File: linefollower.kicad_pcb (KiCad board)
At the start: 2 copper layers, 0 parts

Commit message: Minor schematic fixes - now RC; Basic PCB
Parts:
- added C1: 10uF, Capacitor_SMD:CP_Elec_5x5.3, F.Cu at (53.3, 119.5)
- added C10: 100uF, Capacitor_SMD:CP_Elec_6.3x5.4, F.Cu at (375.3, 51.8)
- added C11: 10uF, Capacitor_SMD:CP_Elec_5x5.3, F.Cu at (135.9, 125.1)
- added C12: 22pF, Capacitor_SMD:C_0805_2012Metric, F.Cu at (401.0, 43.1)
- added C13: 22pF, Capacitor_SMD:C_0805_2012Metric, F.Cu at (401.3, 34.8)
- added C14: 2.2uF, Capacitor_SMD:C_0805_2012Metric, F.Cu at (378.8, 65.0)
- added C15: 2.2uF, Capacitor_SMD:C_0805_2012Metric, F.Cu at (385.5, 58.9)
- added C16: 100nF, Capacitor_SMD:C_0805_2012Metric, F.Cu at (380.2, 61.1)
- added C17: 100nF, Capacitor_SMD:C_0805_2012Metric, F.Cu at (356.3, 78.1)
- added C18: 100nF, Capacitor_SMD:C_0805_2012Metric, F.Cu at (402.7, 32.8)
- added C19: 100nF, Capacitor_SMD:C_0805_2012Metric, F.Cu at (371.2, 68.0)
- added C2: 10uF, Capacitor_SMD:CP_Elec_5x5.3, F.Cu at (384.1, 51.1)
- added C20: 100nF, Capacitor_SMD:C_0805_2012Metric, F.Cu at (363.1, 78.4)
- added C21: 100nF, Capacitor_SMD:C_0805_2012Metric, F.Cu at (389.8, 48.9)
- added C22: 100nF, Capacitor_SMD:C_0805_2012Metric, F.Cu at (401.3, 38.7)
- added C23: 100nF, Capacitor_SMD:C_0805_2012Metric, F.Cu at (401.0, 41.1)
- added C24: 100nF, Capacitor_SMD:C_0805_2012Metric, F.Cu at (389.8, 50.9)
- added C25: 100nF, Capacitor_SMD:C_0805_2012Metric, F.Cu at (393.2, 47.3)
- added C26: 100nF, Capacitor_SMD:C_0805_2012Metric, F.Cu at (397.6, 43.1)
- added C27: 100nF, Capacitor_SMD:C_0805_2012Metric, F.Cu at (375.4, 65.7)
- added C28: 100nF, Capacitor_SMD:C_0805_2012Metric, F.Cu at (378.8, 63.1)
- added C29: 100nF, Capacitor_SMD:C_0805_2012Metric, F.Cu at (352.9, 78.1)
- added C3: 1nF, Capacitor_SMD:C_0805_2012Metric, F.Cu at (374.6, 69.9)
- added C30: 4.7uF, Capacitor_SMD:C_0805_2012Metric, F.Cu at (375.4, 63.8)
- added C31: 1uF, Capacitor_SMD:C_0805_2012Metric, F.Cu at (359.7, 78.4)
- added C32: 6.8pF, Capacitor_SMD:C_0805_2012Metric, F.Cu at (401.3, 36.7)
- added C33: 6.8pF, Capacitor_SMD:C_0805_2012Metric, F.Cu at (397.6, 47.0)
- added C34: 1uF, Capacitor_SMD:C_0805_2012Metric, F.Cu at (375.4, 61.8)
- added C35: 100uF, Capacitor_SMD:CP_Elec_6.3x5.4, F.Cu at (73.1, 132.2)
- added C36: 100uF, Capacitor_SMD:CP_Elec_6.3x5.4, F.Cu at (63.2, 132.2)
- added C4: 100nF, Capacitor_SMD:C_0805_2012Metric, F.Cu at (393.2, 51.2)
- added C5: 100nF, Capacitor_SMD:C_0805_2012Metric, F.Cu at (57.7, 118.8)
- added C6: 100nF, Capacitor_SMD:C_0805_2012Metric, F.Cu at (354.2, 55.3)
- added C7: 100nF, Capacitor_SMD:C_0805_2012Metric, F.Cu at (74.3, 116.0)
- added C8: 100nF, Capacitor_SMD:C_0805_2012Metric, F.Cu at (371.5, 71.9)
- added C9: 100uF, Capacitor_SMD:CP_Elec_6.3x5.4, F.Cu at (76.2, 110.8)
- added D1: LED, LED_SMD:LED_0603_1608Metric, F.Cu at (345.7, 66.3)
- added D2: LED, LED_SMD:LED_0603_1608Metric, F.Cu at (330.2, 72.0)
- added D3: 1N4001, Diode_THT:D_DO-41_SOD81_P10.16mm_Horizontal, F.Cu at (78.3, 126.1)
- added D4: 1N4001, Diode_THT:D_DO-41_SOD81_P10.16mm_Horizontal, F.Cu at (320.4, 74.5)
- added D5: stps2l40u, Diode_SMD:D_SMB, F.Cu at (83.5, 110.8)
- added D6: LED_RGB, LED_SMD:LED_RGB_5050-6, F.Cu at (396.0, 37.4)
- added D7: stps2l40u, Diode_SMD:D_SMB, F.Cu at (128.1, 124.3)
- added F1: MF-SM250, linefollower:MF-MSMF-A, F.Cu at (81.0, 119.9)
- added F2: MF-MSMF050, linefollower:MF-MSMF-A, F.Cu at (126.6, 136.5)
- added J1: BATT, linefollower:Soldered_pad_01x02_4x6, F.Cu at (81.0, 132.1)
- added J10: I2C, Connector_PinSocket_2.54mm:PinSocket_1x04_P2.54mm_Vertical, F.Cu at (347.1, 54.2)
- added J11: BT_module, Connector_PinSocket_2.54mm:PinSocket_1x04_P2.54mm_Vertical, F.Cu at (350.7, 54.2)
- added J12: USB_B_Micro, Connector_USB:USB_Micro-B_Amphenol_10103594-0001LF_Horizontal, F.Cu at (137.0, 132.6)
- added J13: LINE_SENS, Connector_PinHeader_2.54mm:PinHeader_2x19_P2.54mm_Vertical, F.Cu at (235.0, 55.0)
- added J14: Micro_SD_Card_Det, Connector_Card:microSD_HC_Hirose_DM3AT-SF-PEJM5, F.Cu at (343.7, 33.0)
- added J15: Conn_linesens_Female, Connector_PinSocket_2.54mm:PinSocket_1x11_P2.54mm_Horizontal, F.Cu at (332.9, -8.17)
- added J16: Conn_linesens_Male, Connector_PinSocket_2.54mm:PinSocket_1x11_P2.54mm_Horizontal, F.Cu at (320.6, -8.17)
- added J17: Conn_lineboard_Female_PWR0, linefollower:Soldered_pad_01x01_4x6, F.Cu at (335.2, -3.55)
- added J18: Conn_lineboard_Female_PWR1, linefollower:Soldered_pad_01x01_4x6, F.Cu at (349.9, -3.55)
- added J19: Conn_lineboard_Male_PWR0, linefollower:Soldered_pad_01x01_4x6, F.Cu at (345.0, -3.55)
- added J2: 3v3, Connector_PinSocket_2.54mm:PinSocket_1x02_P2.54mm_Vertical, F.Cu at (382.0, 55.8)
- added J20: Conn_lineboard_Male_PWR0, linefollower:Soldered_pad_01x01_4x6, F.Cu at (340.1, -3.55)
- added J21: ESC_MOTOR, linefollower:Soldered_pad_01x03_4x5, B.Cu at (141.8, 93.5)
- added J22: MOTOR_ESC, linefollower:Soldered_pad_01x03_4x5, F.Cu at (129.0, 93.5)
- added J3: 3v3, Connector_PinSocket_2.54mm:PinSocket_1x02_P2.54mm_Vertical, F.Cu at (364.6, 72.9)
- added J4: 5v, Connector_PinSocket_2.54mm:PinSocket_1x02_P2.54mm_Vertical, F.Cu at (371.9, 62.7)
- added J5: SWD+UART, Connector_PinSocket_2.54mm:PinSocket_2x05_P2.54mm_Vertical, F.Cu at (45.2, 81.0)
- added J6: SPI2, Connector_PinSocket_2.54mm:PinSocket_1x06_P2.54mm_Vertical, F.Cu at (353.4, 33.8)
- added J7: I2C, Connector_PinSocket_2.54mm:PinSocket_1x04_P2.54mm_Vertical, F.Cu at (359.1, 47.6)
- added J8: ESC, linefollower:Soldered_pad_01x02_4x6, F.Cu at (93.0, 132.1)
- added J9: ESC_CTRL, Connector_PinSocket_2.54mm:PinSocket_1x02_P2.54mm_Vertical, F.Cu at (394.1, 42.0)
- added JP1: PWR_SELECT, Jumper:SolderJumper-3_P1.3mm_Open_RoundedPad1.0x1.5mm, F.Cu at (83.0, 117.7)
- added JP2: PWR_USB, Connector_PinSocket_2.54mm:PinSocket_1x02_P2.54mm_Vertical, F.Cu at (361.0, 73.1)
- added R1: 10k, Resistor_SMD:R_0805_2012Metric, F.Cu at (315.2, 77.7)
- added R10: 5.6k, Resistor_SMD:R_0805_2012Metric, F.Cu at (389.8, 54.8)
- added R11: 510r, Resistor_SMD:R_0805_2012Metric, F.Cu at (383.6, 61.1)
- added R12: 510r, Resistor_SMD:R_0805_2012Metric, F.Cu at (393.2, 49.2)
- added R13: 510r, Resistor_SMD:R_0805_2012Metric, F.Cu at (389.8, 52.8)
- added R14: 47k, Resistor_SMD:R_0805_2012Metric, F.Cu at (385.5, 56.9)
- added R15: 47k, Resistor_SMD:R_0805_2012Metric, F.Cu at (385.5, 55.0)
- added R16: 47k, Resistor_SMD:R_0805_2012Metric, F.Cu at (325.3, 77.1)
- added R17: 47k, Resistor_SMD:R_0805_2012Metric, F.Cu at (374.6, 68.0)
- added R18: 47k, Resistor_SMD:R_0805_2012Metric, F.Cu at (368.0, 74.0)
- added R19: 10k, Resistor_SMD:R_0805_2012Metric, F.Cu at (368.0, 72.0)
- added R2: 10k, Resistor_SMD:R_0805_2012Metric, F.Cu at (377.7, 37.4)
- added R20: 10k, Resistor_SMD:R_0805_2012Metric, F.Cu at (59.0, 105.7)
- added R21: 22r, Resistor_SMD:R_0805_2012Metric, F.Cu at (126.1, 128.8)
- added R22: 22r, Resistor_SMD:R_0805_2012Metric, F.Cu at (126.1, 130.8)
- added R23: 10k, Resistor_SMD:R_0805_2012Metric, F.Cu at (346.0, 64.6)
- added R24: 10k, Resistor_SMD:R_0805_2012Metric, F.Cu at (371.2, 69.9)
- added R25: 47k, Resistor_SMD:R_0805_2012Metric, F.Cu at (328.7, 77.1)
- added R3: 10k, Resistor_SMD:R_0805_2012Metric, F.Cu at (397.6, 45.0)
- added R4: 10k, Resistor_SMD:R_0805_2012Metric, F.Cu at (349.5, 64.6)
- added R5: 510r, Resistor_SMD:R_0805_2012Metric, F.Cu at (332.2, 77.4)
- added R6: 1k, Resistor_SMD:R_0805_2012Metric, F.Cu at (335.6, 77.4)
- added R7: 1.8k, Resistor_SMD:R_0805_2012Metric, F.Cu at (339.0, 77.4)
- added R8: 510r, Resistor_SMD:R_0805_2012Metric, F.Cu at (381.1, 37.4)
- added R9: 20k, Resistor_SMD:R_0805_2012Metric, F.Cu at (354.2, 53.3)
- added SW1: uBTN_0, Button_Switch_SMD:SW_SPST_FSMSM, F.Cu at (367.3, 46.2)
- added SW2: uBTN_1, Button_Switch_SMD:SW_SPST_FSMSM, F.Cu at (346.5, 69.2)
- added SW3: uBTN_2, Button_Switch_SMD:SW_SPST_FSMSM, F.Cu at (351.3, 50.3)
- added SW4: uBTN_3, Button_Switch_SMD:SW_SPST_FSMSM, F.Cu at (334.6, 69.2)
- added SW5: SW_DIP_x04, Button_Switch_SMD:SW_DIP_SPSTx04_Slide_KingTek_DSHP04TS_W7.62mm_P1.27mm, F.Cu at (346.5, 74.9)
- added SW6: RST, Button_Switch_SMD:SW_SPST_FSMSM, F.Cu at (367.3, 42.2)
- added U1: ACS712xLCTR-30A, Package_SO:SOIC-8_3.9x4.9mm_P1.27mm, F.Cu at (88.3, 123.3)
- added U10: Troyka-IMU10, linefollower:Troyka_IMU, F.Cu at (353.0, 28.1)
- added U11: AltIMU-10v5, linefollower:AltIMU10_v5, F.Cu at (374.2, 24.4)
- added U12: UM7, Connector_JST:JST_SH_BM05B-SRSS-TB_1x05-1MP_P1.00mm_Vertical, F.Cu at (366.6, 58.0)
- added U13: STM32F429ZITx, Package_QFP:LQFP-144_20x20mm_P0.5mm, F.Cu at (64.0, 64.5)
- added U2: L7805, Package_TO_SOT_SMD:TO-263-3_TabPin2, F.Cu at (67.8, 121.8)
- added U3: LM1117-3.3, Package_TO_SOT_SMD:TO-252-3_TabPin2, F.Cu at (381.6, 27.7)
- added U4: IP4220CZ6, Package_SO:TSOP-6_1.65x3.05mm_P0.95mm, F.Cu at (130.9, 129.8)
- added U5: MAX14870_carrier, linefollower:MAX14870_Carrier, F.Cu at (122.2, 101.2)
- added U6: MAX14870_carrier, linefollower:MAX14870_Carrier, F.Cu at (68.0, 101.2)
- added U7: ADG726BSUZ, Package_QFP:TQFP-48-1EP_7x7mm_P0.5mm_EP3.5x3.5mm, F.Cu at (392.4, 29.4)
- added U8: M_R, Connector_JST:JST_SH_BM06B-SRSS-TB_1x06-1MP_P1.00mm_Vertical, F.Cu at (115.0, 106.6)
- added U9: M_L, Connector_JST:JST_SH_BM06B-SRSS-TB_1x06-1MP_P1.00mm_Vertical, F.Cu at (65.0, 106.6)
- added Y1: 8MHz, Crystal:Crystal_SMD_3215-2Pin_3.2x1.5mm, F.Cu at (308.1, 77.9)
- added Y2: 32MHz, Crystal:Crystal_HC49-4H_Vertical, F.Cu at (332.2, 64.3)
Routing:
- net GND: track 0.00 -> 17.5 mm
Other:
- board outline added: 100 x 100 mm
- net class Default: trace_width 0.25 -> 0.2; via_dia 0.8 -> 0.6
- net class ESC added: clearance 0.2, trace_width 1.5, via_dia 1, via_drill 0.7
- net class PWR added: clearance 0.2, trace_width 0.6, via_dia 0.6, via_drill 0.4

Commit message: PCB for linesensor board and powermodule finished
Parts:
- removed C11: 10uF, Capacitor_SMD:CP_Elec_5x5.3
- removed J17: Conn_lineboard_Female_PWR0, linefollower:Soldered_pad_01x01_4x6
- removed J18: Conn_lineboard_Female_PWR1, linefollower:Soldered_pad_01x01_4x6
- removed J19, J20: Conn_lineboard_Male_PWR0, linefollower:Soldered_pad_01x01_4x6
- added C37: 100nF, Capacitor_SMD:C_0805_2012Metric, F.Cu at (245.5, 53.2)
- added C38: 100nF, Capacitor_SMD:C_0805_2012Metric, F.Cu at (45.8, 64.4)
- added D10: LED, LED_SMD:LED_0603_1608Metric, F.Cu at (132.3, 128.0)
- added D8: LED, LED_SMD:LED_0603_1608Metric, F.Cu at (259.5, 46.5)
- added D9: LED, LED_SMD:LED_0603_1608Metric, F.Cu at (220.6, 46.5)
- added R26: 510r, Resistor_SMD:R_0805_2012Metric, F.Cu at (257.4, 46.6)
- added R27: 510r, Resistor_SMD:R_0805_2012Metric, F.Cu at (222.6, 46.6)
- added R28: 510r, Resistor_SMD:R_0805_2012Metric, F.Cu at (129.2, 127.9)
- J13: value LINE_SENS -> Conn_02x20_Odd_Even; footprint Connector_PinHeader_2.54mm:PinHeader_2x19_P2.54mm_Vertical -> Connector_PinSocket_2.54mm:PinSocket_2x20_P2.54mm_Vertical; moved to B.Cu
- J15: footprint Connector_PinSocket_2.54mm:PinSocket_1x11_P2.54mm_Horizontal -> linefollower:SolderedPad_1x11_P2.54
- JP2: footprint Connector_PinSocket_2.54mm:PinSocket_1x02_P2.54mm_Vertical -> Jumper:SolderJumper-2_P1.3mm_Open_RoundedPad1.0x1.5mm
- moved R8 350.8 mm to (43.2, 131.3), turned to 270 degrees
- moved J2 341.3 mm to (49.1, 131.4)
- moved R10 340.6 mm to (55.1, 117.9), turned to 90 degrees
- moved C34 328.8 mm to (46.9, 73.9)
- moved J3 323.9 mm to (46.0, 131.4)
- moved J4 323.3 mm to (56.0, 131.3)
- moved C4 312.3 mm to (88.1, 118.1), turned to 180 degrees
- moved R9 304.0 mm to (57.1, 117.9), turned to 270 degrees
- moved D1 300.3 mm to (53.2, 134.5), turned to 90 degrees
- moved D2 293.7 mm to (43.2, 134.5), turned to 90 degrees
- moved C3 290.2 mm to (88.1, 116.0)
- moved R5 284.1 mm to (53.2, 131.2), turned to 270 degrees
- moved R25 281.9 mm to (46.9, 71.0)
- moved C2 281.2 mm to (114.9, 132.5), turned to 270 degrees
- moved U3 273.5 mm to (124.5, 120.9)
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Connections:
- J13 pad 10: /AIN4 -> /AIN26
- J13 pad 11: /AIN5 -> /AIN23
- J13 pad 12: /AIN6 -> /AIN24
- J13 pad 13: /AIN7 -> /AIN21
- J13 pad 14: /AIN8 -> /AIN22
- J13 pad 15: /AIN9 -> /AIN19
- J13 pad 16: /AIN10 -> /AIN20
- J13 pad 17: /AIN11 -> /AIN17
- J13 pad 18: /AIN12 -> /AIN18
- J13 pad 19: /AIN13 -> /AIN15
- J13 pad 2: Net-(J13-Pad2) -> /LB_GND
- J13 pad 20: /AIN14 -> /AIN16
- J13 pad 21: /AIN15 -> /AIN13
- J13 pad 22: /AIN16 -> /AIN14
- J13 pad 23: /AIN17 -> /AIN11
- J13 pad 24: /AIN18 -> /AIN12
- J13 pad 25: /AIN19 -> /AIN9
- J13 pad 26: /AIN20 -> /AIN10
- J13 pad 27: /AIN21 -> /AIN7
- J13 pad 28: /AIN22 -> /AIN8
- J13 pad 29: /AIN23 -> /AIN5
- J13 pad 3: /LB_3V3 -> /AIN31
- J13 pad 30: /AIN24 -> /AIN6
- J13 pad 31: /AIN25 -> /AIN3
- J13 pad 32: /AIN26 -> /AIN4
- J13 pad 33: /AIN27 -> /AIN1
- J13 pad 34: /AIN28 -> /AIN2
- J13 pad 35: /AIN29 -> /LB_LED_C0
- J13 pad 36: /AIN30 -> /LB_LED_C0
- J13 pad 37: /AIN31 -> /LB_3V3
- J13 pad 38: Net-(J13-Pad38) -> /LB_3V3
- J13 pad 4: Net-(J13-Pad4) -> /LB_3V3
- J13 pad 5: /LB_LED_C0 -> /AIN29
- J13 pad 6: /LB_LED_C0 -> /AIN30
- J13 pad 7: /AIN1 -> /AIN27
- J13 pad 8: /AIN2 -> /AIN28
- J13 pad 9: /AIN3 -> /AIN25
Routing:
- net GND: track 17.5 -> 0.00 mm
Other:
- board size 100 x 100 mm -> 229.2 x 107 mm

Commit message: MCU's main peripherals PCB
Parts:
- added ?: MountingHole_2.2mm_M2_ISO7380, MountingHole:MountingHole_2.2mm_M2_ISO7380, F.Cu at (86.8, 89.1)
- added ?: MountingHole_2.2mm_M2_ISO7380, MountingHole:MountingHole_2.2mm_M2_ISO7380, F.Cu at (93.2, 89.1)
- added ?: MountingHole_2.2mm_M2_ISO7380, MountingHole:MountingHole_2.2mm_M2_ISO7380, F.Cu at (93.2, 95.5)
- added ?: MountingHole_2.2mm_M2_ISO7380, MountingHole:MountingHole_2.2mm_M2_ISO7380, F.Cu at (86.8, 95.5)
- moved J10 378.2 mm to (-30.9, 65.3)
- moved J11 378.2 mm to (-27.3, 65.3)
- moved J14 378.2 mm to (-34.4, 44.2)
- moved J16 378.2 mm to (-57.5, 3.00)
- moved R1 378.2 mm to (-62.8, 88.9)
- moved R12 378.2 mm to (15.1, 60.4)
- moved R13 378.2 mm to (11.7, 64.0)
- moved R17 378.2 mm to (-3.44, 79.2)
- moved R18 378.2 mm to (-10.0, 85.2)
- moved R2 378.2 mm to (-0.34, 48.6)
- moved R3 378.2 mm to (19.5, 56.2)
- moved R4 378.2 mm to (-28.6, 75.7)
- moved U11 378.2 mm to (-3.87, 35.6)
- moved U12 378.2 mm to (-11.5, 69.2)
- moved D6 378.2 mm to (17.9, 48.5)
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- renumbered J9 to J9-ESC
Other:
- outline, holes or cut-outs redrawn
- board text added: "RESET"

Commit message: All PCB components places
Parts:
- removed ? (x4): MountingHole_2.2mm_M2_ISO7380, MountingHole:MountingHole_2.2mm_M2_ISO7380
- removed J9-ESC: ESC_CTRL, Connector_PinSocket_2.54mm:PinSocket_1x02_P2.54mm_Vertical
- added G***: LOGO, linefollower:letovo, F.Cu at (119.8, 81.0)
- added J9: ESC_CTRL, Connector_PinSocket_2.54mm:PinSocket_1x02_P2.54mm_Vertical, F.Cu at (46.6, 124.6)
- added REF**: ESD-Logo_8.9x8mm_SilkScreen, Symbol:ESD-Logo_8.9x8mm_SilkScreen, F.Cu at (101.1, 115.0)
- moved R1 184.9 mm to (118.9, 54.7), turned to 180 degrees
- moved D8 176.2 mm to (109.1, -45.5)
- moved J15 176.2 mm to (71.9, 31.2)
- moved R27 176.2 mm to (72.3, -45.4)
- moved U7 176.2 mm to (89.8, -43.3)
- moved D9 176.2 mm to (70.3, -45.5)
- moved J13 176.2 mm to (65.7, -54.8)
- moved R26 176.2 mm to (107.1, -45.4)
- moved C37 175.9 mm to (95.5, -38.8)
- moved R16 173.6 mm to (120.1, 72.5), turned to 180 degrees
- moved J14 167.1 mm to (131.1, 67.6), turned to 90 degrees
- moved R4 151.4 mm to (119.0, 42.1), turned to 180 degrees
- moved J7 146.0 mm to (122.3, 95.6), turned to 270 degrees
- moved J10 144.6 mm to (113.4, 73.7), turned to 270 degrees
- moved SW5 144.0 mm to (110.5, 62.9), turned to 180 degrees
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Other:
- board size 229.2 x 107 mm -> 100 x 199 mm
- board text added: "BATTERY 12V"
- board text added: "BOOT0"
- board text added: "BOOT1"
- board text added: "Bardin Petr Zaripov Vadim Zorin Kirill"
- board text added: "DOWN"
- board text added: "ENTER"
- board text added: "ESC"
- board text added: "I2C"
- board text added: "MENU"
- board text added: "OLED"
- board text added: "PG0"
- board text added: "PG1"
- board text added: "SPI2"
- board text added: "SWD/UART"
- board text added: "UART6"
- board text added: "UP"

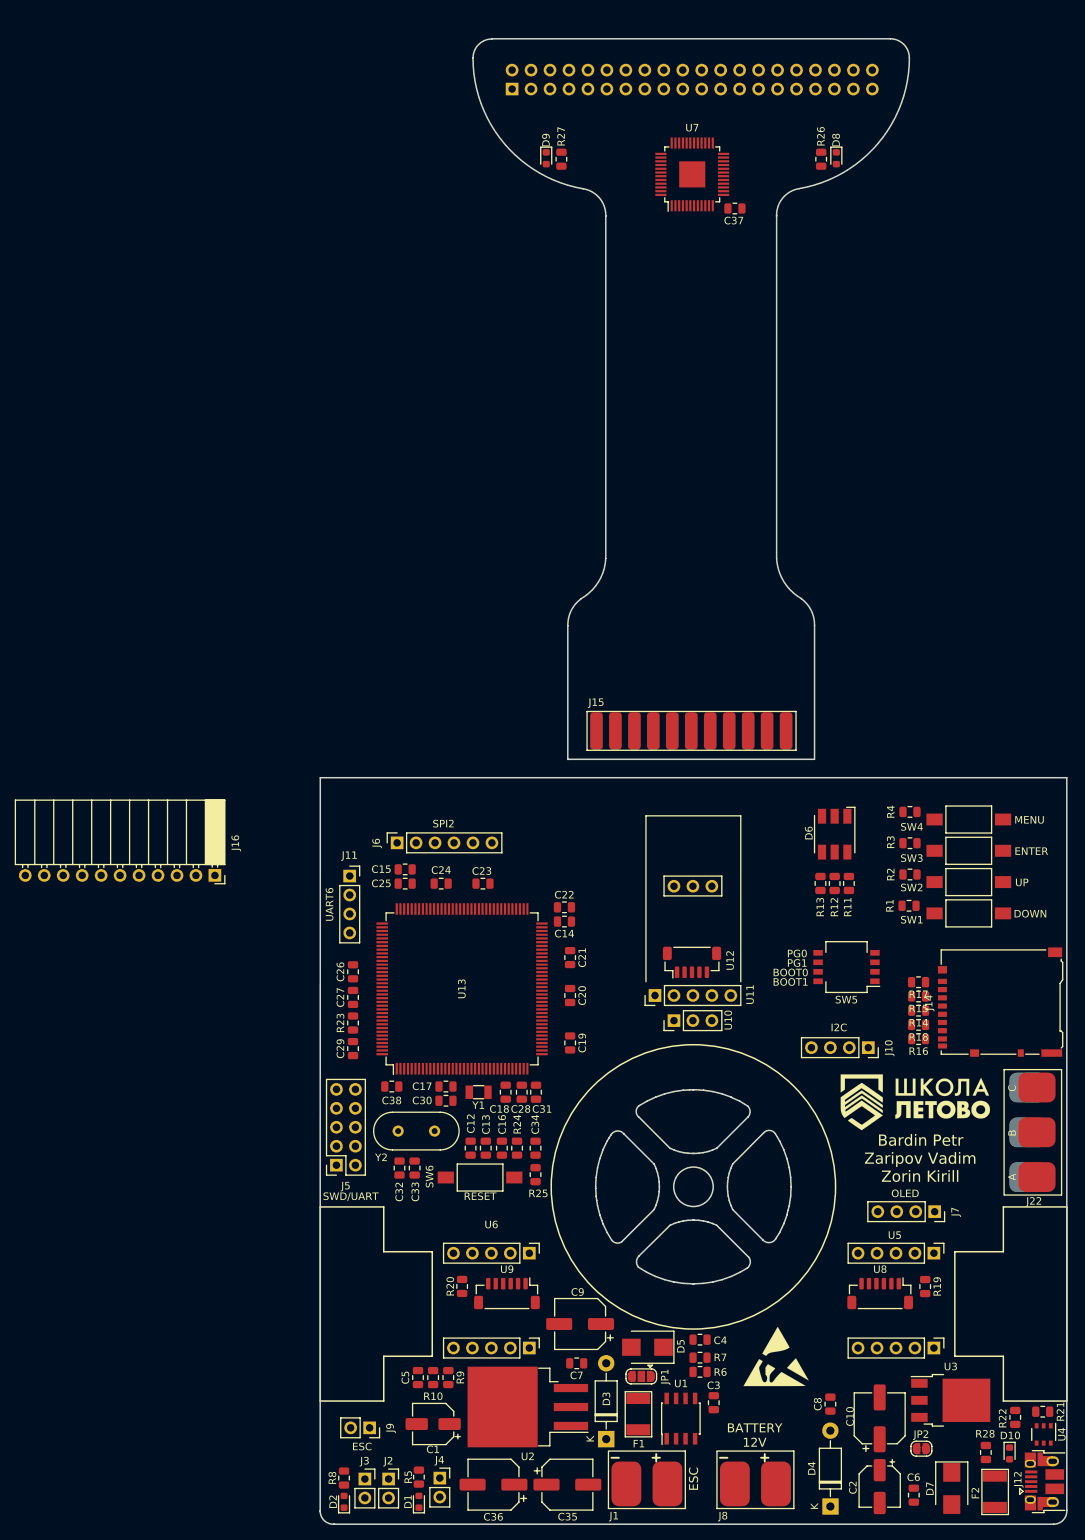
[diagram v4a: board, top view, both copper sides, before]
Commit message: Finished connection of PCBs
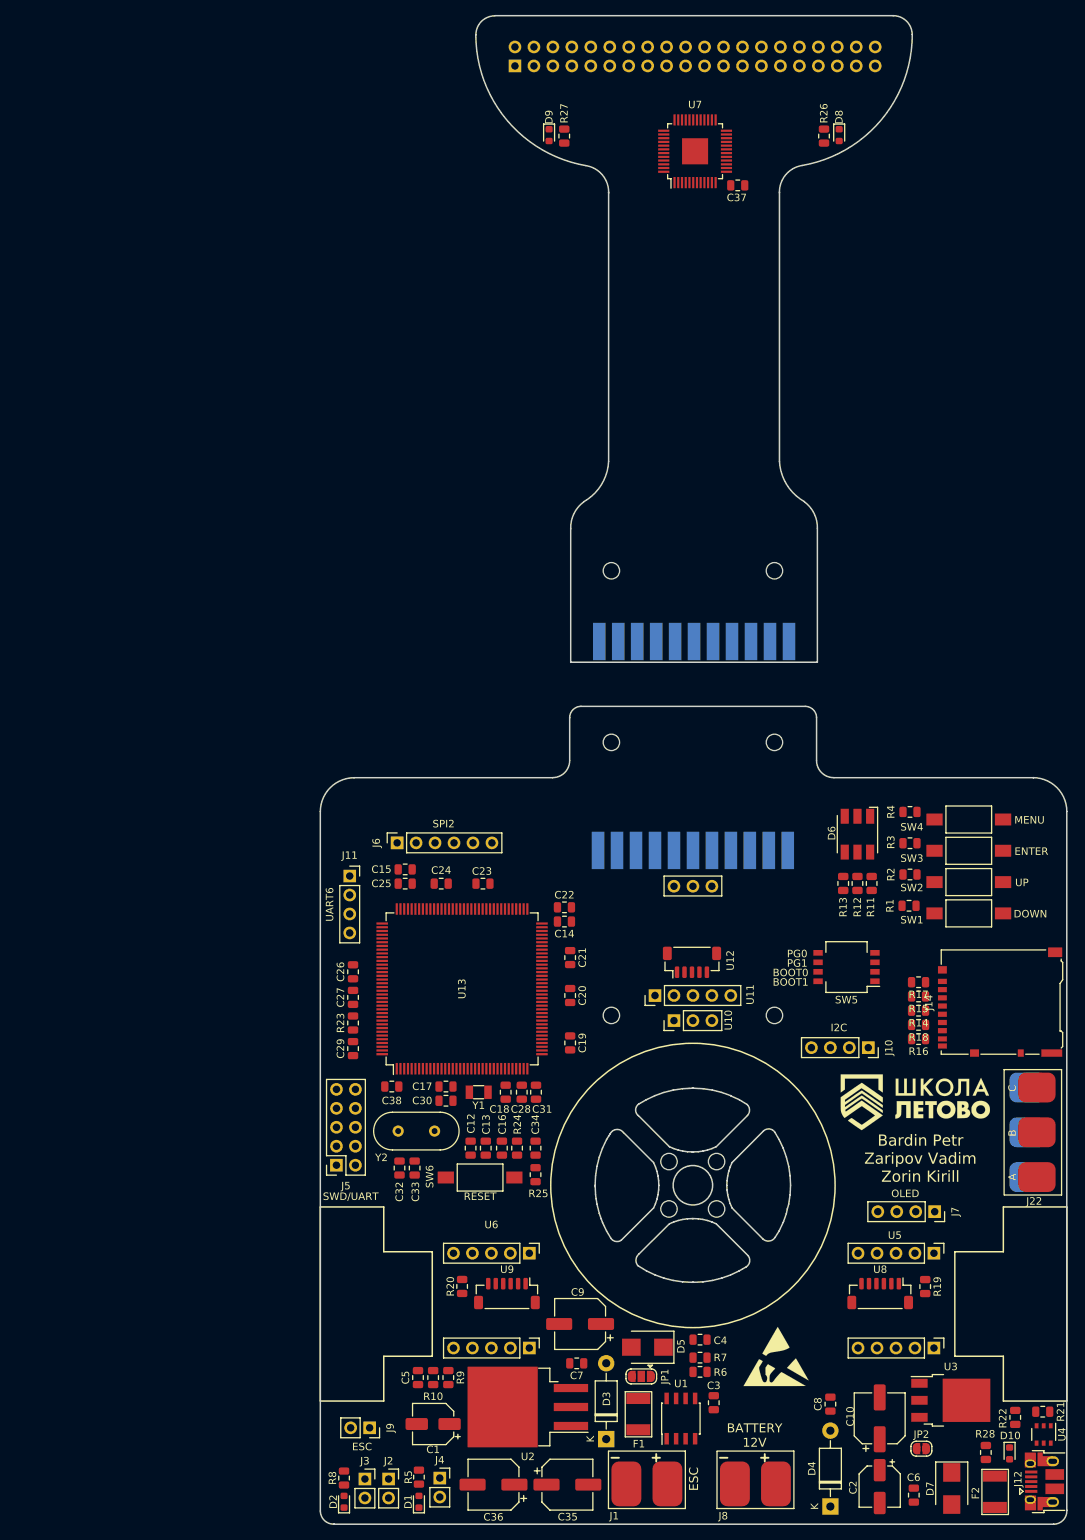
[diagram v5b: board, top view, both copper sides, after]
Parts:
- added ?: MountingHole_2.2mm_M2, MountingHole:MountingHole_2.2mm_M2, F.Cu at (100.8, 9.78)
- added ?: MountingHole_2.2mm_M2, MountingHole:MountingHole_2.2mm_M2, F.Cu at (79.0, 69.3)
- added ?: MountingHole_2.2mm_M2, MountingHole:MountingHole_2.2mm_M2, F.Cu at (79.0, 9.78)
- added ?: MountingHole_2.2mm_M2, MountingHole:MountingHole_2.2mm_M2, F.Cu at (79.0, 32.8)
- added ?: MountingHole_2.2mm_M2, MountingHole:MountingHole_2.2mm_M2, F.Cu at (100.8, 32.8)
- added ?: MountingHole_2.2mm_M2, MountingHole:MountingHole_2.2mm_M2, F.Cu at (100.8, 69.3)
- added ?: MountingHole_2.2mm_M2_ISO7380, MountingHole:MountingHole_2.2mm_M2_ISO7380, F.Cu at (86.7, 88.9)
- added ?: MountingHole_2.2mm_M2_ISO7380, MountingHole:MountingHole_2.2mm_M2_ISO7380, F.Cu at (93.1, 88.9)
- added ?: MountingHole_2.2mm_M2_ISO7380, MountingHole:MountingHole_2.2mm_M2_ISO7380, F.Cu at (93.1, 95.3)
- added ?: MountingHole_2.2mm_M2_ISO7380, MountingHole:MountingHole_2.2mm_M2_ISO7380, F.Cu at (86.7, 95.3)
- J15: moved to B.Cu
- J16: footprint Connector_PinSocket_2.54mm:PinSocket_1x11_P2.54mm_Horizontal -> linefollower:SolderedPad_1x11_P2.54; moved to B.Cu
- moved J16 46.4 mm to (72.1, 47.2)
- moved J15 12.0 mm to (72.3, 19.3), turned to 270 degrees
- moved C37 3.12 mm to (95.9, -41.8)
- moved R26 3.12 mm to (107.5, -48.5)
- moved R27 3.12 mm to (72.7, -48.5)
- moved D8 3.12 mm to (109.5, -48.6)
- moved D9 3.12 mm to (70.6, -48.6)
- moved J13 3.12 mm to (66.1, -57.9)
- moved U7 3.12 mm to (90.2, -46.4)
- moved D6 3.05 mm to (112.0, 45.1)
- moved R11 3.05 mm to (113.9, 51.7)
- moved R12 3.05 mm to (112.0, 51.7)
- moved R13 3.05 mm to (110.1, 51.7)
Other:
- board size 100 x 199 mm -> 100 x 202.1 mm

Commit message: PCB minor improvements
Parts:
- moved MH10 138.1 mm to (181.1, 122.1)
- moved MH9 138.1 mm to (159.3, 122.1)
- moved C37 138.1 mm to (176.2, 70.5)
- moved D8 138.1 mm to (189.8, 63.7)
- moved D9 138.1 mm to (150.9, 63.7)
- moved J13 138.1 mm to (146.4, 54.5)
- moved J15 138.1 mm to (152.6, 131.6)
- moved R26 138.1 mm to (187.8, 63.9)
- moved R27 138.1 mm to (153.0, 63.9)
- moved U7 138.1 mm to (170.5, 65.9)
- turned C26 to 270 degrees
- gave numbers to parts that had none: 10
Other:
- board size 100 x 202.1 mm -> 159.6 x 109.6 mm
- net class PWR: trace_width 0.6 -> 0.35
